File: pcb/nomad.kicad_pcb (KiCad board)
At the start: 2 copper layers, 65 x 120 mm, 78 parts, among them J1 USB_C_Receptacle_USB2.0_16P, J2 Conn_01x08_Pin, J3 Conn_Coaxial, J4 Conn_Coaxial, J5 Conn_01x02_Pin, Q2 2N7002, SW1 UP, SW2 DOWN, SW3 RIGHT, SW4 LEFT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

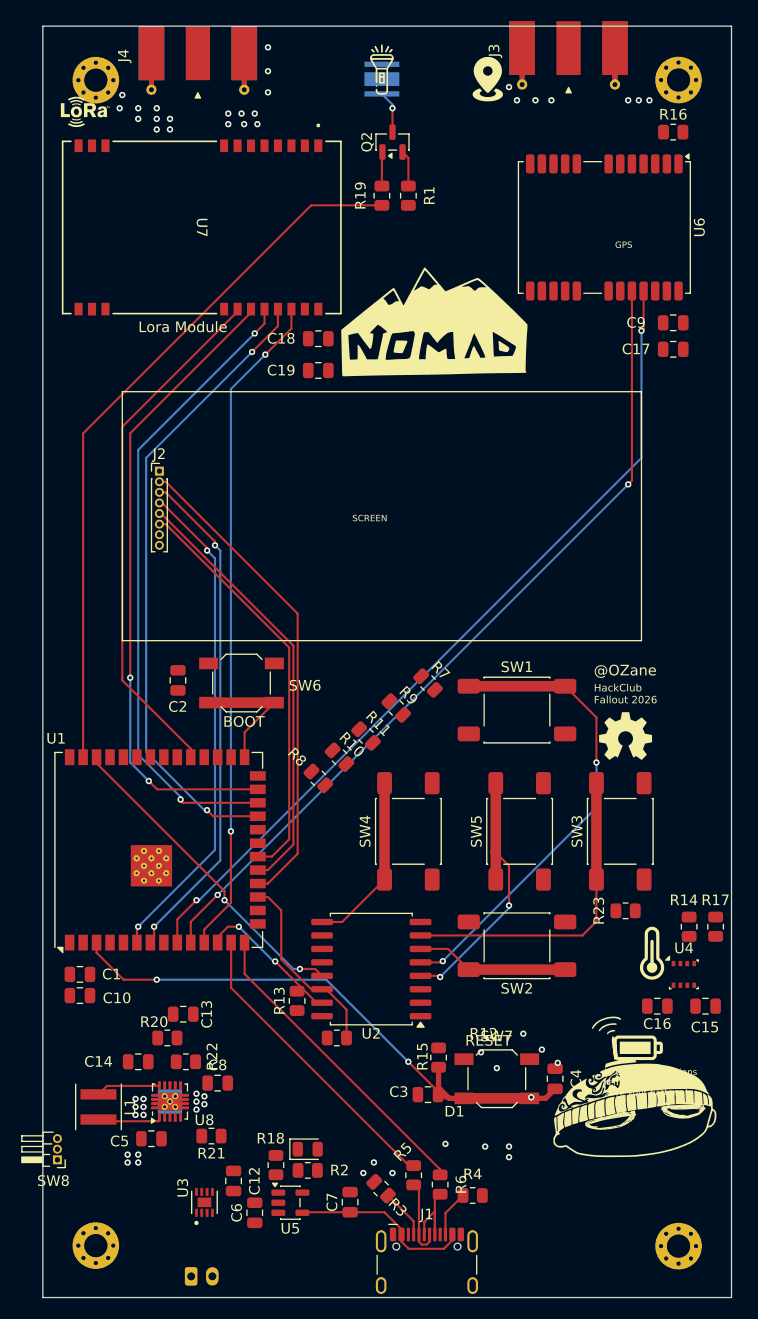
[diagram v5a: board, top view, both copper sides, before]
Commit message: Finishing routing
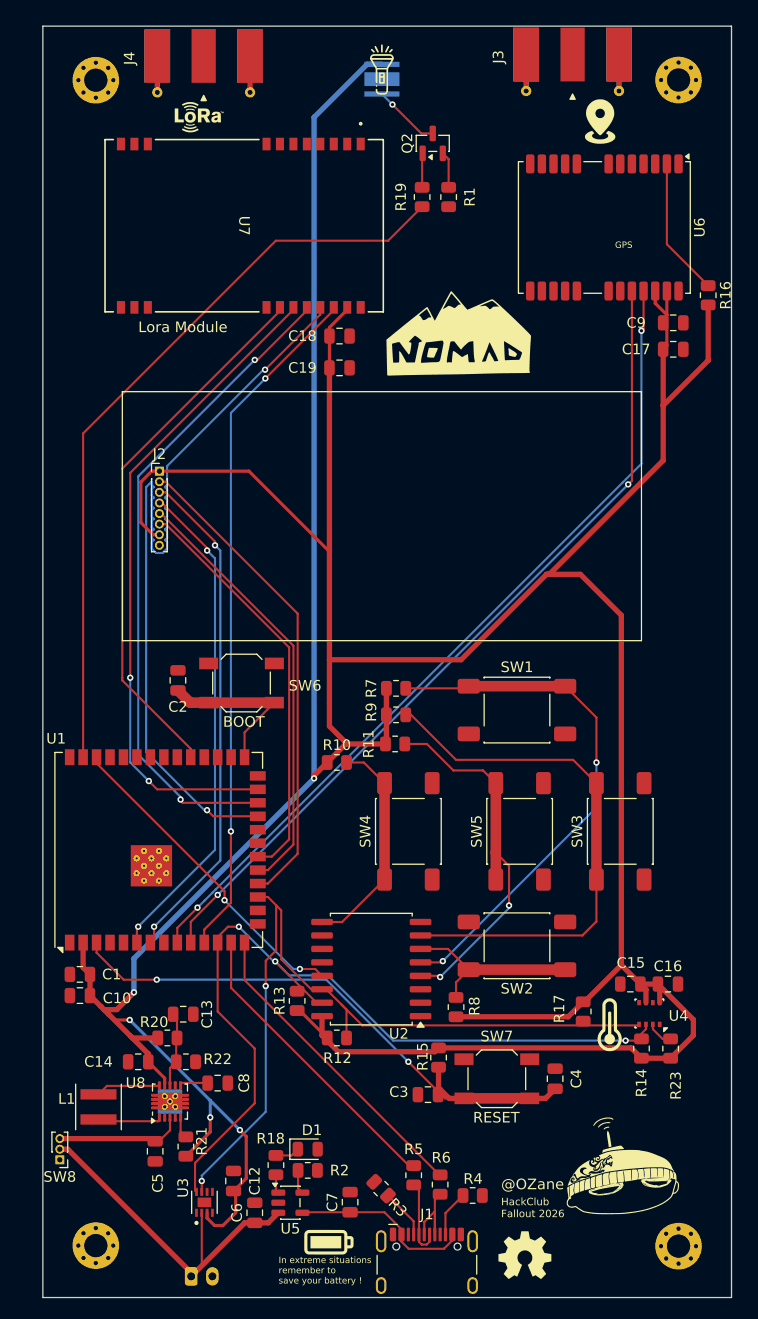
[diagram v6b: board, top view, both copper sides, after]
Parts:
- SW8: footprint Connector_PinHeader_1.00mm:PinHeader_1x03_P1.00mm_Horizontal -> Connector_PinHeader_1.00mm:PinHeader_1x03_P1.00mm_Vertical
- moved G*** 49.9 mm to (145.5, 161.0)
- moved G*** 40.9 mm to (155.1, 154.8)
- moved G*** 34.5 mm to (127.0, 159.8)
- moved R8 25.2 mm to (139.0, 137.6), turned to 90 degrees
- moved R16 15.7 mm to (162.8, 70.4), turned to -90 degrees
- moved R17 14.8 mm to (151.0, 138.0), turned to -90 degrees
- moved R23 13.7 mm to (159.2, 141.5), turned to 90 degrees
- moved R14 12.3 mm to (156.5, 141.5), turned to 90 degrees
- moved G*** 11.3 mm to (152.6, 54.0)
- moved G*** 10.8 mm to (114.8, 53.5)
- moved G*** 7.85 mm to (153.5, 139.2)
- moved C15 7.40 mm to (155.4, 135.4), turned to 180 degrees
- moved U4 4.92 mm to (157.2, 138.2), turned to 180 degrees
- moved U7 4.00 mm to (119.0, 63.8)
- moved Q2 3.80 mm to (136.8, 56.1)
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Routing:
- net +3V3: track 0.00 -> 426.0 mm, vias 0 -> 5
- net SDA: track 13.8 -> 80.1 mm, vias 2 -> 3
- net SCL: track 18.2 -> 77.1 mm, vias 0 -> 2
- net +BATT: track 0.00 -> 34.7 mm
- net BTN_RIGHT: track 30.2 -> 51.0 mm
- net LORA_MI: track 60.0 -> 77.7 mm
- net Net-(U6-D_SEL): track 0.00 -> 13.1 mm
- net Net-(SW8-C): track 0.00 -> 11.2 mm
- net BTN_SEL: track 26.0 -> 36.4 mm
- net Net-(U8-FB): track 0.00 -> 6.90 mm
- net BTN_UP: track 44.4 -> 50.9 mm
- net BTN_LEFT: track 16.7 -> 21.1 mm
- net FLASHLIGHT: track 67.7 -> 71.4 mm
- net BOOT: track 12.5 -> 15.9 mm
- net BTN_DOWN: track 14.5 -> 17.6 mm
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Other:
- board text removed: "SCREEN"

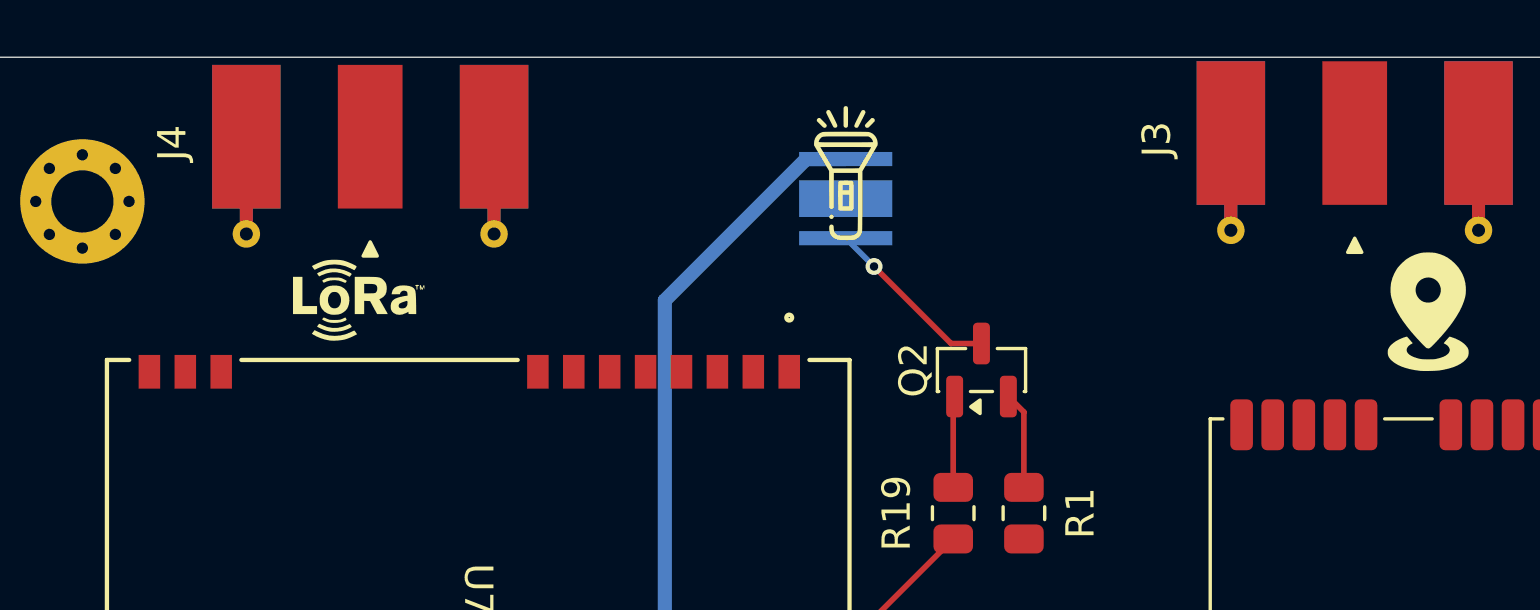
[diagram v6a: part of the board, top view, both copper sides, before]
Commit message: Adding 50ohms traces
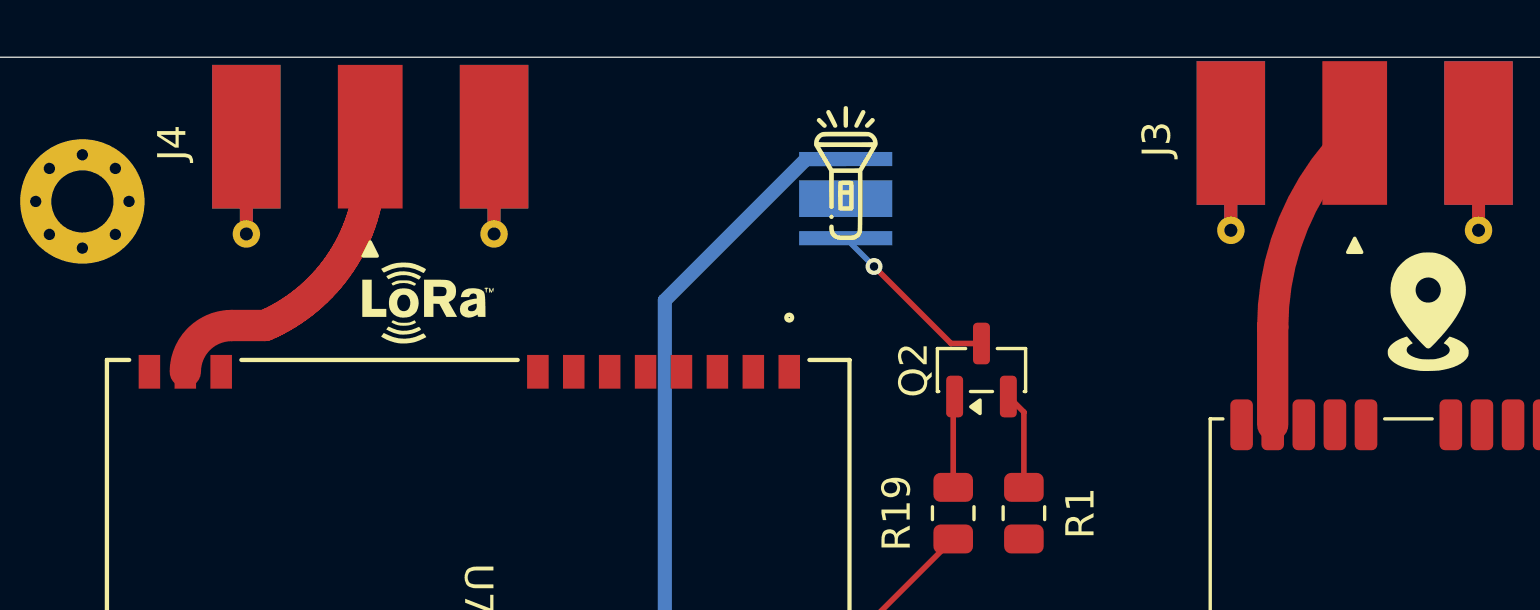
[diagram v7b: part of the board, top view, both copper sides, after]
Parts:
- moved G*** 2.45 mm to (117.2, 53.6)
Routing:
- net Net-(J3-In): track 0.00 -> 12.5 mm
- net Net-(J4-In): track 0.00 -> 11.9 mm
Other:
- board text removed: "USB-C > charging IC > JST > MAX > Buck boost"

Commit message: Finishing PCB
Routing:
- net GND: track 0.00 -> 25.4 mm, vias 0 -> 146
- net +5V: track 17.2 -> 24.2 mm
- net Net-(SW8-C): track 11.2 -> 13.1 mm
- net Net-(J4-In): vias 0 -> 1
- added copper zone on B.Cu, net GND
- added copper zone on F.Cu, net GND
